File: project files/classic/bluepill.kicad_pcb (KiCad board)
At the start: 2 copper layers, 53.3 x 22.9 mm, 36 parts, among them J1 USB_B_Micro, J2 Boot, J3 Left Row, J4 SWD, J5 Right Row, SW1 Reset, U1 RT8183-33, U2 STM32F103C8Tx, Y1 8MHz, Y2 32768Hz

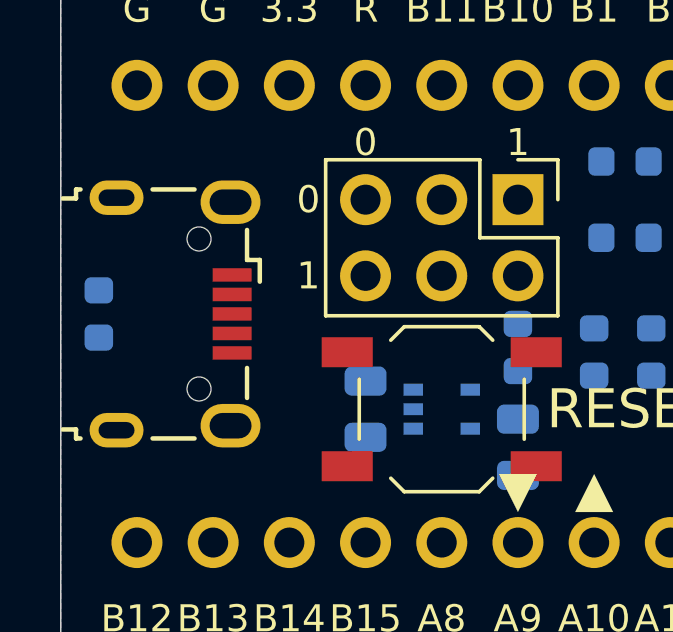
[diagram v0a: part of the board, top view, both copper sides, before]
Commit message: Updates after re-opening in KiCAD 5.1.7
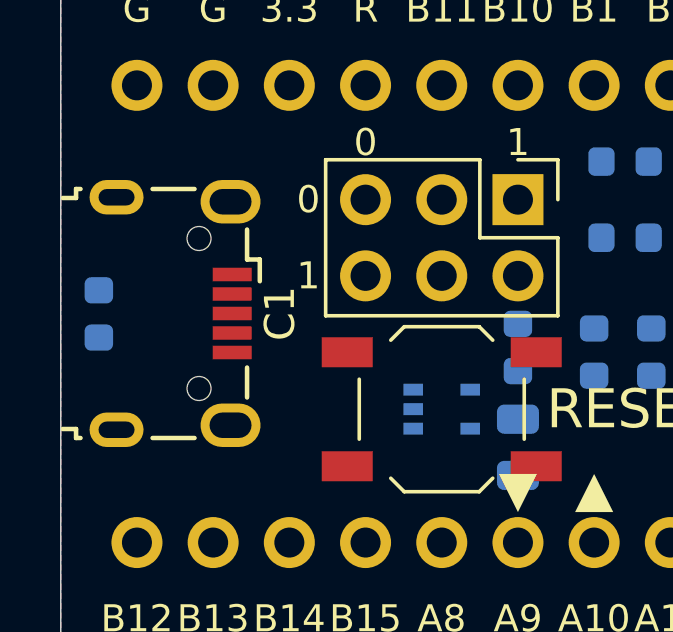
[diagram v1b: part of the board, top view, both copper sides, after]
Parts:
- removed J1: USB_B_Micro, Connector_USB:USB_Micro-B_Wuerth_629105150521
- C1: footprint Capacitor_SMD:C_0805_2012Metric -> Connector_USB:USB_Micro-B_Wuerth_629105150521; moved to F.Cu
- moved C1 7.11 mm to (110.5, 125.7)
